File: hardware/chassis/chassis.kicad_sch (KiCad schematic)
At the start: 108 parts, among them J1 RJ45_LED_Shielded, Q1 SiR422DP, Q2 Si7898DP, Q3 MMDT3906, T1 PoE_Transformer, T2 Pulse_Transformer, U1 TPS23754PWPR, U2 TCMT1107, U3 TCMT1107, U4 KSZ8081RND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

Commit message: hardware: prepare for more KiCad projects
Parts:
- J1: footprint chassis:RJHSE-538X -> common:RJHSE-538X; symbol chassis:RJ45_LED_SHEILDED -> common:RJ45_LED_SHEILDED
- Q1: symbol chassis:SiR422DP -> common:SiR422DP
- Q2: symbol chassis:Si7898DP -> common:Si7898DP
- T1: footprint chassis:POE_EP13 -> common:POE_EP13; symbol chassis:PoE_Transformer -> common:PoE_Transformer
- T2: footprint chassis:GDTI_EP7 -> common:GDTI_EP7; symbol chassis:Pulse_Transformer -> common:Pulse_Transformer
- U1: footprint Package_SO:HTSSOP-20-1EP_4.4x6.5mm_P0.65mm_EP3.4x6.5mm -> common:TSSOP-20; symbol chassis:TPS23754PWPR -> common:TPS23754PWPR
- U4: footprint chassis:QFN-24 -> common:QFN-24
- U6: footprint chassis:QFP-64 -> common:QFP-64; symbol chassis:EFM32GG11B8xx -> common:EFM32GG11B8xx
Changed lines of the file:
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@@
     )
   )
-  (symbol (lib_id "chassis:EFM32GG11B8xx") (at 73.66 170.18 0) (unit 1)
+  (symbol (lib_id "common:EFM32GG11B8xx") (at 73.66 170.18 0) (unit 1)
     (in_bom yes) (on_board yes)
     (property "Reference" "U6" (id 0) (at 45.72 124.46 0)
@@
       (effects (font (size 1.27 1.27)) (justify right))
     )
-    (property "Footprint" "chassis:QFP-64" (id 2) (at 45.72 125.73 0)
+    (property "Footprint" "common:QFP-64" (id 2) (at 45.72 125.73 0)
       (effects (font (size 1.27 1.27)) hide)
     )
@@
       (effects (font (size 1.27 1.27)) (justify right))
     )
-    (property "Footprint" "chassis:QFN-24" (id 2) (at 228.6 165.1 0)
+    (property "Footprint" "common:QFN-24" (id 2) (at 228.6 165.1 0)
       (effects (font (size 1.27 1.27)) hide)
     )
@@
     (pin "2")
   )
-  (symbol (lib_id "chassis:RJ45_LED_SHEILDED") (at 53.34 38.1 0) (unit 1)
+  (symbol (lib_id "common:RJ45_LED_SHEILDED") (at 53.34 38.1 0) (unit 1)
     (in_bom yes) (on_board yes)
     (property "Reference" "J1" (id 0) (at 53.34 21.1582 0))
     (property "Value" "RJ45_LED_Shielded" (id 1) (at 53.34 23.4696 0))
-    (property "Footprint" "chassis:RJHSE-538X" (id 2) (at 53.34 37.465 90)
+    (property "Footprint" "common:RJHSE-538X" (id 2) (at 53.34 37.465 90)
       (effects (font (size 1.27 1.27)) hide)
     )
@@
     (pin "1")
   )
-  (symbol (lib_id "chassis:TPS23754PWPR") (at 205.74 53.34 0) (unit 1)
+  (symbol (lib_id "common:TPS23754PWPR") (at 205.74 53.34 0) (unit 1)
     (in_bom yes) (on_board yes)
     (property "Reference" "U1" (id 0) (at 205.74 35.8902 0)
@@
       (effects (font (size 1.524 1.524)))
     )
-    (property "Footprint" "Package_SO:HTSSOP-20-1EP_4.4x6.5mm_P0.65mm_EP3.4x6.5mm" (id 2) (at 205.74 81.28 0)
+    (property "Footprint" "common:TSSOP-20" (id 2) (at 205.74 81.28 0)
       (effects (font (size 1.524 1.524)) hide)
     )
@@
     (pin "1")
   )
-  (symbol (lib_id "chassis:PoE_Transformer") (at 320.04 35.56 0) (unit 1)
+  (symbol (lib_id "common:PoE_Transformer") (at 320.04 35.56 0) (unit 1)
     (in_bom yes) (on_board yes)
     (property "Reference" "T1" (id 0) (at 320.04 20.8026 0))
     (property "Value" "PoE_Transformer" (id 1) (at 320.04 23.114 0))
-    (property "Footprint" "chassis:POE_EP13" (id 2) (at 320.04 35.56 0)
+    (property "Footprint" "common:POE_EP13" (id 2) (at 320.04 50.8 0)
       (effects (font (size 1.27 1.27)) hide)
     )
-    (property "Datasheet" "~" (id 3) (at 320.04 35.56 0)
+    (property "Datasheet" "" (id 3) (at 320.04 35.56 0)
       (effects (font (size 1.27 1.27)) hide)
     )
@@
     (pin "1")
   )
-  (symbol (lib_id "chassis:Pulse_Transformer") (at 320.04 78.74 0) (unit 1)
+  (symbol (lib_id "common:Pulse_Transformer") (at 320.04 78.74 0) (unit 1)
     (in_bom yes) (on_board yes)
     (property "Reference" "T2" (id 0) (at 320.04 69.0626 0))
     (property "Value" "Pulse_Transformer" (id 1) (at 320.04 71.374 0))
-    (property "Footprint" "chassis:GDTI_EP7" (id 2) (at 320.04 78.74 0)
+    (property "Footprint" "common:GDTI_EP7" (id 2) (at 320.04 78.74 0)
       (effects (font (size 1.27 1.27)) hide)
     )
@@
     (pin "6")
   )
-  (symbol (lib_id "chassis:Si7898DP") (at 292.1 66.04 0) (unit 1)
+  (symbol (lib_id "common:Si7898DP") (at 292.1 66.04 0) (unit 1)
     (in_bom yes) (on_board yes)
     (property "Reference" "Q2" (id 0) (at 297.3324 64.8716 0)
@@
     (pin "5")
   )
-  (symbol (lib_id "chassis:SiR422DP") (at 344.17 50.8 90) (unit 1)
+  (symbol (lib_id "common:SiR422DP") (at 344.17 50.8 90) (unit 1)
     (in_bom yes) (on_board yes)
     (property "Reference" "Q1" (id 0) (at 344.17 42.0878 90))
@@
     )
     (path "/00000000-0000-0000-0000-00005bbacfd1"
-      (reference "J1") (unit 1) (value "RJ45_LED_Shielded") (footprint "chassis:RJHSE-538X")
+      (reference "J1") (unit 1) (value "RJ45_LED_Shielded") (footprint "common:RJHSE-538X")
     )
     (path "/00000000-0000-0000-0000-00005c1b084a"
@@
     )
     (path "/00000000-0000-0000-0000-00005dad1b8a"
-      (reference "T1") (unit 1) (value "PoE_Transformer") (footprint "chassis:POE_EP13")
+      (reference "T1") (unit 1) (value "PoE_Transformer") (footprint "common:POE_EP13")
     )
     (path "/00000000-0000-0000-0000-00005ef704e4"
-      (reference "T2") (unit 1) (value "Pulse_Transformer") (footprint "chassis:GDTI_EP7")
+      (reference "T2") (unit 1) (value "Pulse_Transformer") (footprint "common:GDTI_EP7")
     )
     (path "/00000000-0000-0000-0000-00005e1b9e90"
@@
     )
     (path "/00000000-0000-0000-0000-00005d69703c"
-      (reference "U1") (unit 1) (value "TPS23754PWPR") (footprint "Package_SO:HTSSOP-20-1EP_4.4x6.5mm_P0.65mm_EP3.4x6.5mm")
+      (reference "U1") (unit 1) (value "TPS23754PWPR") (footprint "common:TSSOP-20")
     )
     (path "/00000000-0000-0000-0000-00005db76b4b"
@@
     )
     (path "/00000000-0000-0000-0000-00005bba24e6"
-      (reference "U4") (unit 1) (value "KSZ8081RND") (footprint "chassis:QFN-24")
+      (reference "U4") (unit 1) (value "KSZ8081RND") (footprint "common:QFN-24")
     )
     (path "/00000000-0000-0000-0000-00005e62130d"
@@
     )
     (path "/00000000-0000-0000-0000-00005bba203b"
-      (reference "U6") (unit 1) (value "EFM32GG11B8xx") (footprint "chassis:QFP-64")
+      (reference "U6") (unit 1) (value "EFM32GG11B8xx") (footprint "common:QFP-64")
     )
     (path "/00000000-0000-0000-0000-00005db66ae6"

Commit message: chassis: correct a number of footprints
These all mistakenly used an 0402 package:
D1, C2, C3, C4, C6, C7, C8, C12, L1, L2, R2, R12
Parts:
- C2, C7, C8: footprint Capacitor_SMD:C_0402_1005Metric -> Capacitor_SMD:C_Elec_8x10.2
- C3, C4: footprint Capacitor_SMD:C_0402_1005Metric -> Capacitor_SMD:C_0805_2012Metric
- C6: footprint Capacitor_SMD:C_0402_1005Metric -> Capacitor_SMD:C_Elec_6.3x7.7
- D1: footprint Diode_SMD:D_0402_1005Metric -> Diode_SMD:D_SMB
- L1, L2: footprint Inductor_SMD:L_0402_1005Metric -> Inductor_SMD:L_Abracon_ASPI-0630LR
- R12, R2: footprint Resistor_SMD:R_0402_1005Metric -> Resistor_SMD:R_0805_2012Metric
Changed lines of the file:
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@@
       (effects (font (size 1.27 1.27)) (justify left))
     )
-    (property "Footprint" "Capacitor_SMD:C_0402_1005Metric" (id 2) (at 252.4252 35.56 0)
+    (property "Footprint" "Capacitor_SMD:C_0805_2012Metric" (id 2) (at 252.4252 35.56 0)
       (effects (font (size 1.27 1.27)) hide)
     )
@@
       (effects (font (size 1.27 1.27)) (justify left))
     )
-    (property "Footprint" "Capacitor_SMD:C_0402_1005Metric" (id 2) (at 262.5852 35.56 0)
+    (property "Footprint" "Capacitor_SMD:C_0805_2012Metric" (id 2) (at 262.5852 35.56 0)
       (effects (font (size 1.27 1.27)) hide)
     )
@@
     (property "Reference" "L1" (id 0) (at 245.11 19.685 90))
     (property "Value" "3u3" (id 1) (at 245.11 21.9964 90))
-    (property "Footprint" "Inductor_SMD:L_0402_1005Metric" (id 2) (at 245.11 25.4 0)
+    (property "Footprint" "Inductor_SMD:L_Abracon_ASPI-0630LR" (id 2) (at 245.11 25.4 0)
       (effects (font (size 1.27 1.27)) hide)
     )
@@
       (effects (font (size 1.27 1.27)) hide)
     )
-    (property "Footprint" "Diode_SMD:D_0402_1005Metric" (id 2) (at 288.29 38.1 0)
+    (property "Footprint" "Diode_SMD:D_SMB" (id 2) (at 288.29 38.1 0)
       (effects (font (size 1.27 1.27)) hide)
     )
@@
       (effects (font (size 1.27 1.27)) (justify left))
     )
-    (property "Footprint" "Resistor_SMD:R_0402_1005Metric" (id 2) (at 270.002 31.75 90)
+    (property "Footprint" "Resistor_SMD:R_0805_2012Metric" (id 2) (at 270.002 31.75 90)
       (effects (font (size 1.27 1.27)) hide)
     )
@@
       (effects (font (size 1.27 1.27)) (justify left))
     )
-    (property "Footprint" "Capacitor_SMD:C_0402_1005Metric" (id 2) (at 238.76 31.75 0)
+    (property "Footprint" "Capacitor_SMD:C_Elec_8x10.2" (id 2) (at 238.76 31.75 0)
       (effects (font (size 1.27 1.27)) hide)
     )
@@
     (property "Reference" "R12" (id 0) (at 300.99 78.74 90))
     (property "Value" "0R18" (id 1) (at 300.99 76.2 90))
-    (property "Footprint" "Resistor_SMD:R_0402_1005Metric" (id 2) (at 300.99 71.882 90)
+    (property "Footprint" "Resistor_SMD:R_0805_2012Metric" (id 2) (at 300.99 71.882 90)
       (effects (font (size 1.27 1.27)) hide)
     )
@@
     (property "Reference" "L2" (id 0) (at 383.54 24.765 90))
     (property "Value" "0u33" (id 1) (at 383.54 27.0764 90))
-    (property "Footprint" "Inductor_SMD:L_0402_1005Metric" (id 2) (at 383.54 30.48 0)
+    (property "Footprint" "Inductor_SMD:L_Abracon_ASPI-0630LR" (id 2) (at 383.54 30.48 0)
       (effects (font (size 1.27 1.27)) hide)
     )
@@
       (effects (font (size 1.27 1.27)) (justify left))
     )
-    (property "Footprint" "Capacitor_SMD:C_0402_1005Metric" (id 2) (at 361.6452 39.37 0)
+    (property "Footprint" "Capacitor_SMD:C_Elec_6.3x7.7" (id 2) (at 361.6452 39.37 0)
       (effects (font (size 1.27 1.27)) hide)
     )
@@
       (effects (font (size 1.27 1.27)) (justify left))
     )
-    (property "Footprint" "Capacitor_SMD:C_0402_1005Metric" (id 2) (at 373.38 35.56 0)
+    (property "Footprint" "Capacitor_SMD:C_Elec_8x10.2" (id 2) (at 373.38 35.56 0)
       (effects (font (size 1.27 1.27)) hide)
     )
@@
       (effects (font (size 1.27 1.27)) (justify left))
     )
-    (property "Footprint" "Capacitor_SMD:C_0402_1005Metric" (id 2) (at 393.7 35.56 0)
+    (property "Footprint" "Capacitor_SMD:C_Elec_8x10.2" (id 2) (at 393.7 35.56 0)
       (effects (font (size 1.27 1.27)) hide)
     )
@@
     )
     (path "/00000000-0000-0000-0000-00005c52fe8e"
-      (reference "C2") (unit 1) (value "47u") (footprint "Capacitor_SMD:C_0402_1005Metric")
+      (reference "C2") (unit 1) (value "47u") (footprint "Capacitor_SMD:C_Elec_8x10.2")
     )
     (path "/00000000-0000-0000-0000-00005c1307f9"
-      (reference "C3") (unit 1) (value "1u") (footprint "Capacitor_SMD:C_0402_1005Metric")
+      (reference "C3") (unit 1) (value "1u") (footprint "Capacitor_SMD:C_0805_2012Metric")
     )
     (path "/00000000-0000-0000-0000-00005c130863"
-      (reference "C4") (unit 1) (value "1u") (footprint "Capacitor_SMD:C_0402_1005Metric")
+      (reference "C4") (unit 1) (value "1u") (footprint "Capacitor_SMD:C_0805_2012Metric")
     )
     (path "/00000000-0000-0000-0000-00005c1f3127"
@@
     )
     (path "/00000000-0000-0000-0000-00005d269bfc"
-      (reference "C6") (unit 1) (value "141u") (footprint "Capacitor_SMD:C_0402_1005Metric")
+      (reference "C6") (unit 1) (value "141u") (footprint "Capacitor_SMD:C_Elec_6.3x7.7")
     )
     (path "/00000000-0000-0000-0000-00005d2f3e39"
-      (reference "C7") (unit 1) (value "330u") (footprint "Capacitor_SMD:C_0402_1005Metric")
+      (reference "C7") (unit 1) (value "330u") (footprint "Capacitor_SMD:C_Elec_8x10.2")
     )
     (path "/00000000-0000-0000-0000-00005d35bf9e"
-      (reference "C8") (unit 1) (value "330u") (footprint "Capacitor_SMD:C_0402_1005Metric")
+      (reference "C8") (unit 1) (value "330u") (footprint "Capacitor_SMD:C_Elec_8x10.2")
     )
     (path "/00000000-0000-0000-0000-00005d3d83f8"
@@
     )
     (path "/00000000-0000-0000-0000-00005c1cc06c"
-      (reference "D1") (unit 1) (value "D") (footprint "Diode_SMD:D_0402_1005Metric")
+      (reference "D1") (unit 1) (value "D") (footprint "Diode_SMD:D_SMB")
     )
     (path "/00000000-0000-0000-0000-00005c2d040b"
@@
     )
     (path "/00000000-0000-0000-0000-00005c1b084a"
-      (reference "L1") (unit 1) (value "3u3") (footprint "Inductor_SMD:L_0402_1005Metric")
+      (reference "L1") (unit 1) (value "3u3") (footprint "Inductor_SMD:L_Abracon_ASPI-0630LR")
     )
     (path "/00000000-0000-0000-0000-00005d269ada"
-      (reference "L2") (unit 1) (value "0u33") (footprint "Inductor_SMD:L_0402_1005Metric")
+      (reference "L2") (unit 1) (value "0u33") (footprint "Inductor_SMD:L_Abracon_ASPI-0630LR")
     )
     (path "/00000000-0000-0000-0000-00005bd57438"
@@
     )
     (path "/00000000-0000-0000-0000-00005c1d8e4a"
-      (reference "R2") (unit 1) (value "39K") (footprint "Resistor_SMD:R_0402_1005Metric")
+      (reference "R2") (unit 1) (value "39K") (footprint "Resistor_SMD:R_0805_2012Metric")
     )
     (path "/00000000-0000-0000-0000-00005d1f72be"
@@
     )
     (path "/00000000-0000-0000-0000-00005c5b8bbf"
-      (reference "R12") (unit 1) (value "0R18") (footprint "Resistor_SMD:R_0402_1005Metric")
+      (reference "R12") (unit 1) (value "0R18") (footprint "Resistor_SMD:R_0805_2012Metric")
     )
     (path "/00000000-0000-0000-0000-00005dba29a0"

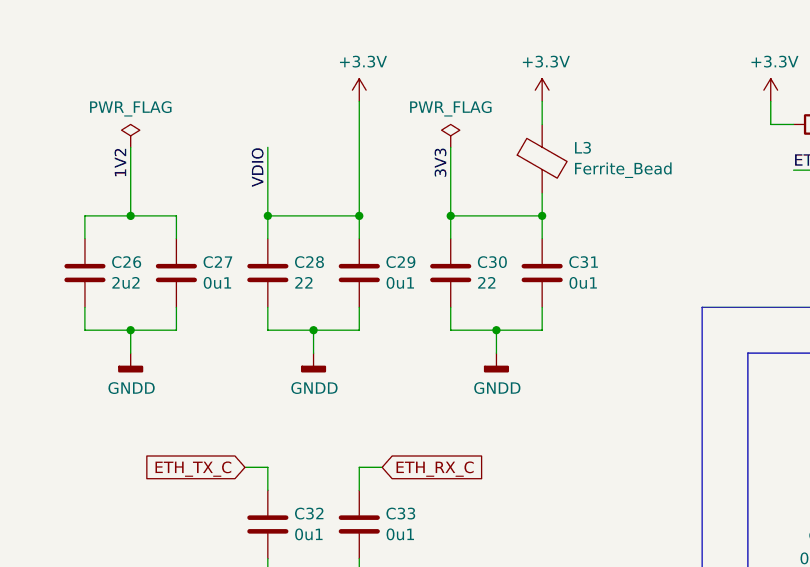
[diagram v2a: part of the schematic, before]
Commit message: chassis: fix value suffix and footprint for C28 and C30
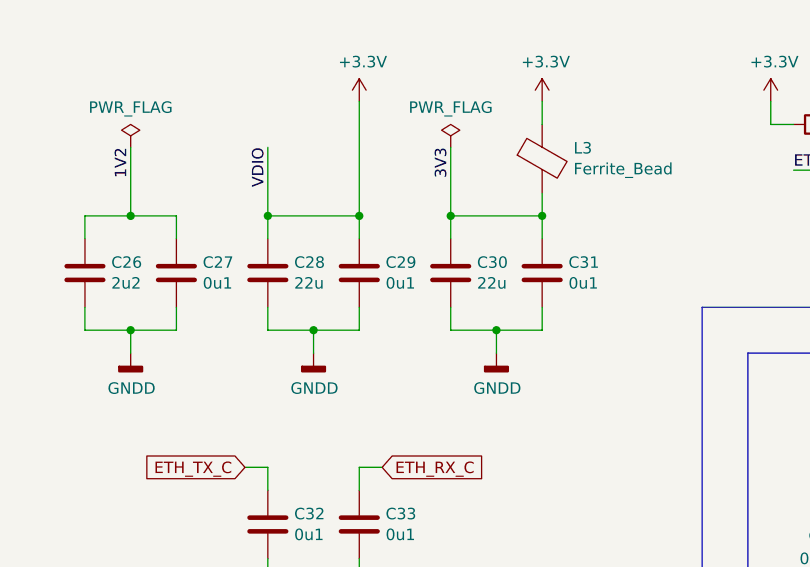
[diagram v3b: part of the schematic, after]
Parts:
- C12: footprint Capacitor_SMD:C_0402_1005Metric -> Capacitor_SMD:C_Elec_5x5.4
- C28, C30: value 22 -> 22u; footprint Capacitor_SMD:C_0402_1005Metric -> Capacitor_SMD:C_0805_2012Metric
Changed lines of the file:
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@@
       (effects (font (size 1.27 1.27)) (justify left))
     )
-    (property "Value" "22" (id 1) (at 264.541 129.413 0)
-      (effects (font (size 1.27 1.27)) (justify left))
-    )
-    (property "Footprint" "Capacitor_SMD:C_0402_1005Metric" (id 2) (at 262.5852 132.08 0)
+    (property "Value" "22u" (id 1) (at 264.541 129.413 0)
+      (effects (font (size 1.27 1.27)) (justify left))
+    )
+    (property "Footprint" "Capacitor_SMD:C_0805_2012Metric" (id 2) (at 262.5852 132.08 0)
       (effects (font (size 1.27 1.27)) hide)
     )
@@
       (effects (font (size 1.27 1.27)) (justify left))
     )
-    (property "Value" "22" (id 1) (at 284.861 129.413 0)
-      (effects (font (size 1.27 1.27)) (justify left))
-    )
-    (property "Footprint" "Capacitor_SMD:C_0402_1005Metric" (id 2) (at 282.9052 132.08 0)
+    (property "Value" "22u" (id 1) (at 284.861 129.413 0)
+      (effects (font (size 1.27 1.27)) (justify left))
+    )
+    (property "Footprint" "Capacitor_SMD:C_0805_2012Metric" (id 2) (at 282.9052 132.08 0)
       (effects (font (size 1.27 1.27)) hide)
     )
@@
       (effects (font (size 1.27 1.27)) (justify left))
     )
-    (property "Footprint" "Capacitor_SMD:C_0402_1005Metric" (id 2) (at 270.51 52.07 0)
+    (property "Footprint" "Capacitor_SMD:C_Elec_5x5.4" (id 2) (at 270.51 52.07 0)
       (effects (font (size 1.27 1.27)) hide)
     )
@@
     )
     (path "/00000000-0000-0000-0000-00005c52ff6b"
-      (reference "C12") (unit 1) (value "22u") (footprint "Capacitor_SMD:C_0402_1005Metric")
+      (reference "C12") (unit 1) (value "22u") (footprint "Capacitor_SMD:C_Elec_5x5.4")
     )
     (path "/00000000-0000-0000-0000-00005bda597d"
@@
     )
     (path "/00000000-0000-0000-0000-00005bd5a75e"
-      (reference "C28") (unit 1) (value "22") (footprint "Capacitor_SMD:C_0402_1005Metric")
+      (reference "C28") (unit 1) (value "22u") (footprint "Capacitor_SMD:C_0805_2012Metric")
     )
     (path "/00000000-0000-0000-0000-00005bd5a757"
@@
     )
     (path "/00000000-0000-0000-0000-00005bd62c33"
-      (reference "C30") (unit 1) (value "22") (footprint "Capacitor_SMD:C_0402_1005Metric")
+      (reference "C30") (unit 1) (value "22u") (footprint "Capacitor_SMD:C_0805_2012Metric")
     )
     (path "/00000000-0000-0000-0000-00005bd62c2c"

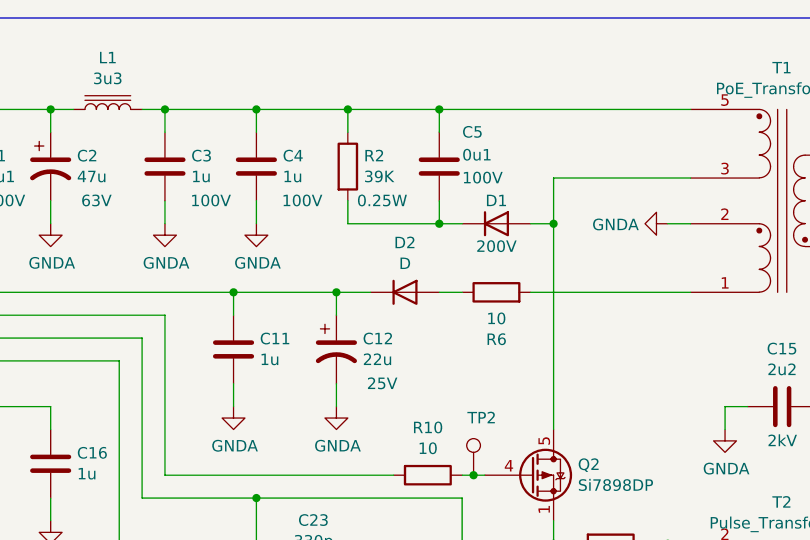
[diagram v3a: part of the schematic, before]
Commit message: chassis: update footprint for D2 and hide value in schematic
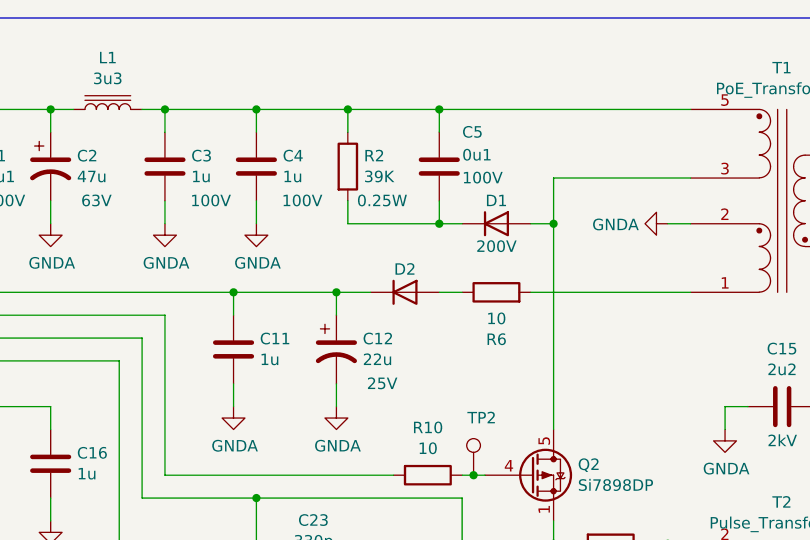
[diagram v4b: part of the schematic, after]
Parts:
- D2: footprint Diode_SMD:D_0402_1005Metric -> Diode_SMD:D_SOD-323
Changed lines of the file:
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@@
   (symbol (lib_id "Device:D") (at 278.13 45.72 0) (unit 1)
     (in_bom yes) (on_board yes)
-    (property "Reference" "D2" (id 0) (at 278.13 40.2336 0))
-    (property "Value" "D" (id 1) (at 278.13 42.545 0))
-    (property "Footprint" "Diode_SMD:D_0402_1005Metric" (id 2) (at 278.13 45.72 0)
+    (property "Reference" "D2" (id 0) (at 278.13 43.18 0))
+    (property "Value" "D" (id 1) (at 278.13 42.545 0)
+      (effects (font (size 1.27 1.27)) hide)
+    )
+    (property "Footprint" "Diode_SMD:D_SOD-323" (id 2) (at 278.13 45.72 0)
       (effects (font (size 1.27 1.27)) hide)
     )
@@
     )
     (path "/00000000-0000-0000-0000-00005c2d040b"
-      (reference "D2") (unit 1) (value "D") (footprint "Diode_SMD:D_0402_1005Metric")
+      (reference "D2") (unit 1) (value "D") (footprint "Diode_SMD:D_SOD-323")
     )
     (path "/00000000-0000-0000-0000-00005c00f7a7"
